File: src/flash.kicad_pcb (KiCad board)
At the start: 2 copper layers, 5 parts, among them J1 Conn_01x06, J2 Conn_01x06, U2 W25Q128JVS

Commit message: feat: add board scheme
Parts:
- R1: footprint Resistor_THT:R_Axial_DIN0411_L9.9mm_D3.6mm_P25.40mm_Horizontal -> Resistor_THT:R_Axial_DIN0411_L9.9mm_D3.6mm_P12.70mm_Horizontal
- moved R1 90.9 mm to (167.0, 65.3), turned to 90 degrees
- moved J1 73.6 mm to (152.5, 52.9)
- moved J2 72.9 mm to (156.5, 53.0)
- moved D1 72.4 mm to (160.5, 65.0)
- moved U2 70.7 mm to (161.6, 56.1), turned to 90 degrees
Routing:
- net /MOSI: track 0.00 -> 53.5 mm
- net /3V3: track 0.00 -> 25.5 mm
- net /SCK: track 0.00 -> 20.6 mm
- net /CS: track 0.00 -> 12.1 mm
- net /MISO: track 0.00 -> 11.3 mm
- net Net-(D1-A): track 0.00 -> 4.14 mm
- added copper zone on F.Cu, net GND
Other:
- board outline added: 20 x 20 mm

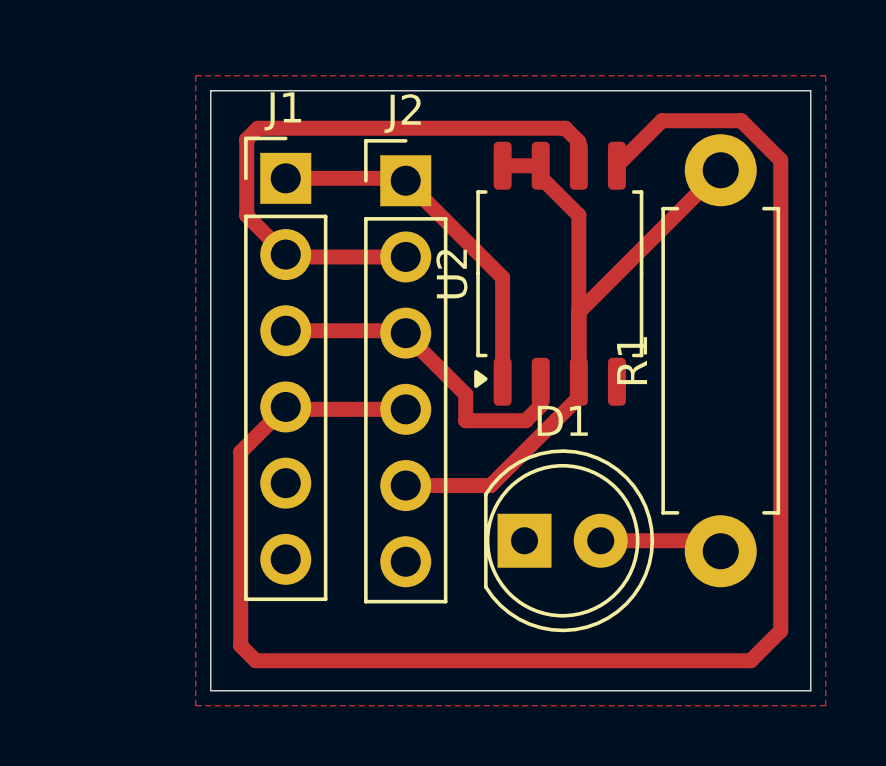
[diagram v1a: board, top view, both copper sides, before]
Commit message: fix: remove GND fill, edit flash routes
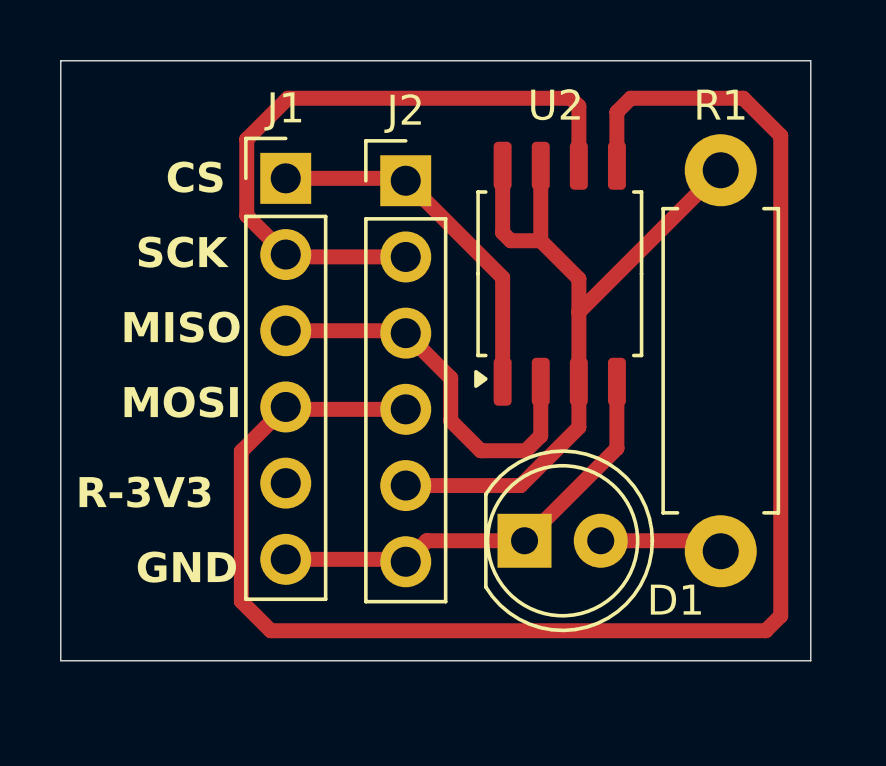
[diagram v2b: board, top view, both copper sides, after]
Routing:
- net GND: track 0.11 -> 14.9 mm
- net /MISO: track 11.3 -> 13.0 mm
- net /SCK: track 20.6 -> 22.1 mm
- net /3V3: track 25.5 -> 26.1 mm
- removed copper zone on F.Cu, net GND
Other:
- board size 20 x 20 mm -> 25 x 20 mm
- board text added: "CS"
- board text added: "GND"
- board text added: "MISO"
- board text added: "MOSI"
- board text added: "R-3V3"
- board text added: "SCK"

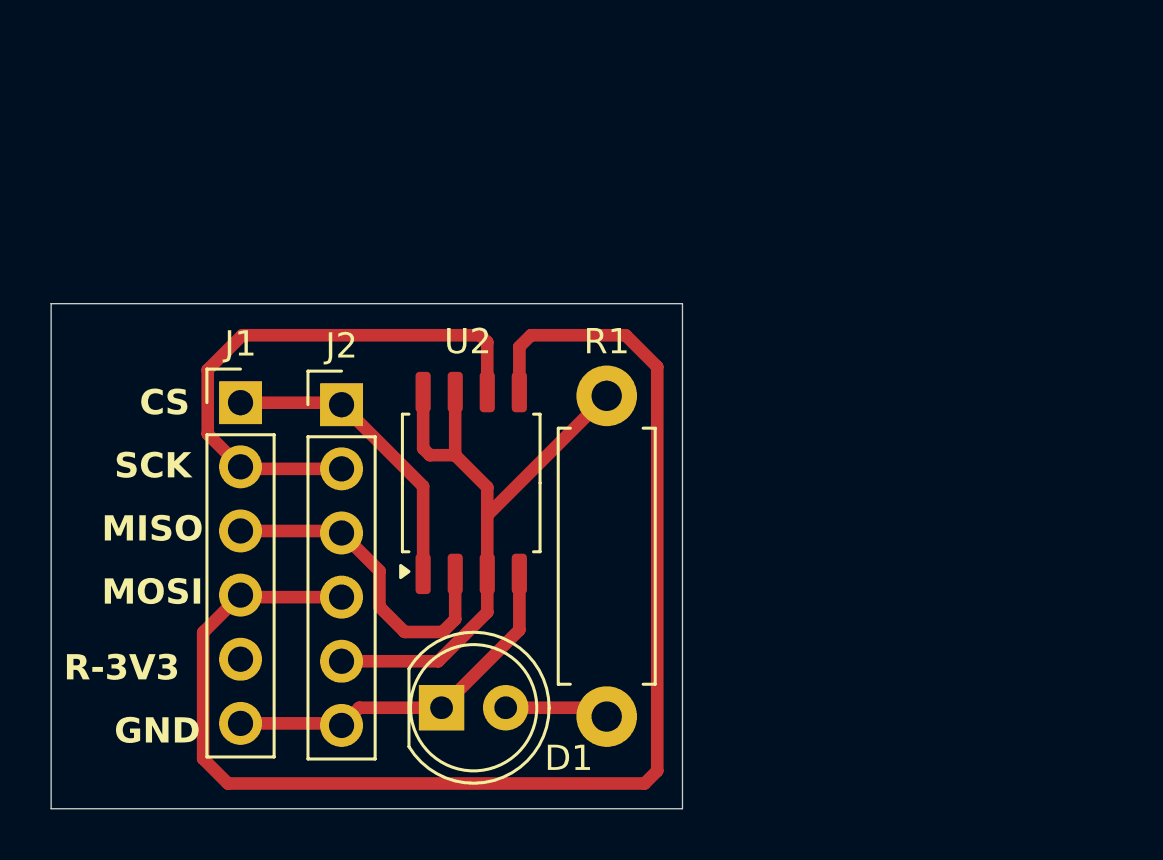
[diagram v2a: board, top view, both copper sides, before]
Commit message: feat: bigger size
Bigger size for comfortable production
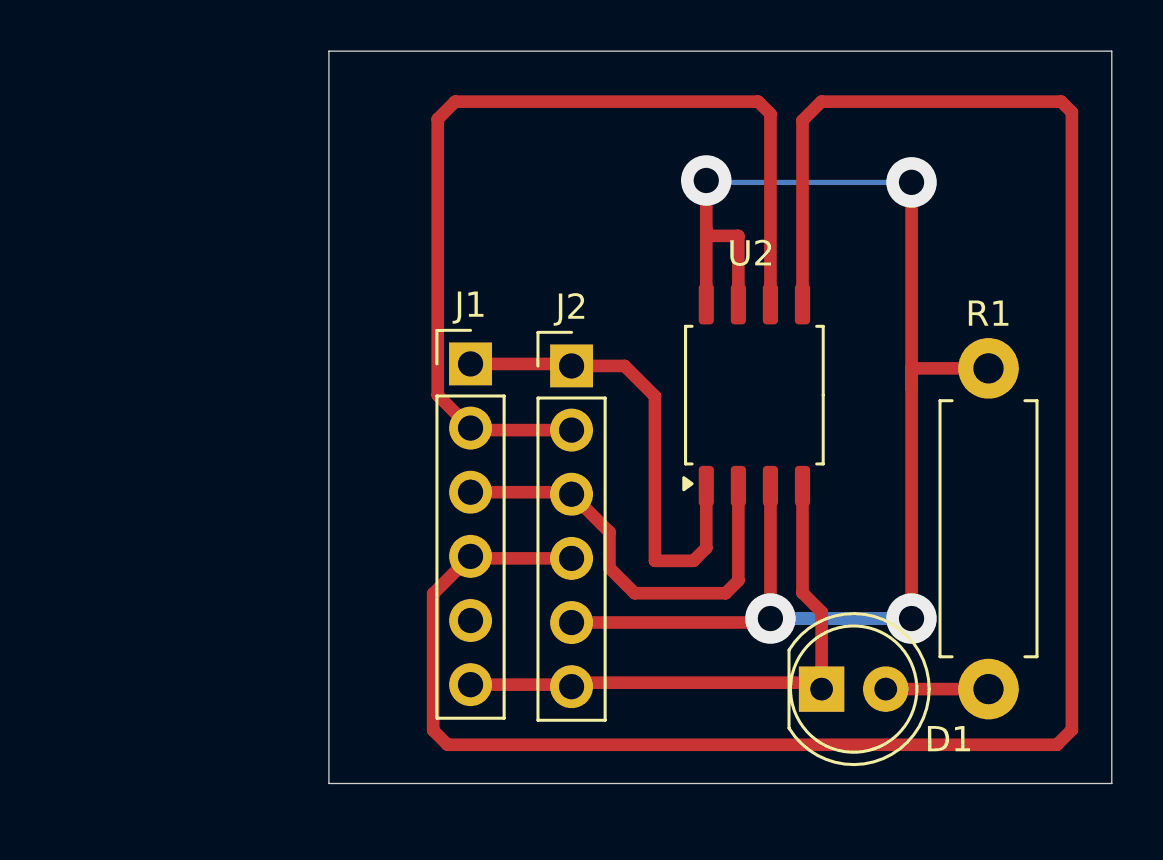
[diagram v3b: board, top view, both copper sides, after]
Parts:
- moved R1 15.2 mm to (182.1, 64.3)
- moved D1 15.1 mm to (175.5, 64.3)
- moved U2 11.7 mm to (172.8, 52.6)
- moved J1 9.24 mm to (161.6, 51.4)
- moved J2 9.24 mm to (165.6, 51.5)
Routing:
- net /3V3: track 26.1 -> 57.4 mm, vias 0 -> 4
- net /MOSI: track 53.7 -> 80.2 mm
- net /SCK: track 22.1 -> 38.0 mm
- net GND: track 14.9 -> 22.5 mm
- net /CS: track 12.1 -> 19.0 mm
- net /MISO: track 13.0 -> 17.1 mm
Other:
- board size 25 x 20 mm -> 31 x 29 mm
- board text removed: "CS"
- board text removed: "GND"
- board text removed: "MISO"
- board text removed: "MOSI"
- board text removed: "R-3V3"
- board text removed: "SCK"

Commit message: fix: more space for dev
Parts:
- moved J1 3.81 mm to (157.8, 51.4)
- moved J2 3.81 mm to (161.8, 51.5)
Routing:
- net GND: track 22.5 -> 163.7 mm, vias 0 -> 6
- net /MOSI: track 80.2 -> 87.4 mm
- net /SCK: track 38.0 -> 43.5 mm
- net /MISO: track 17.1 -> 21.2 mm
- net /3V3: track 57.4 -> 61.2 mm
- net /CS: track 19.0 -> 22.4 mm
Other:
- board size 31 x 29 mm -> 45 x 40 mm
